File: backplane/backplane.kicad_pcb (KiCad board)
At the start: 2 copper layers, 100 x 100 mm, 14 parts, among them J1 Conn_02x16_Row_Letter_First, J2 Conn_02x16_Row_Letter_First, J3 Conn_02x16_Row_Letter_First, J4 Conn_02x16_Row_Letter_First, J5 Conn_02x16_Row_Letter_First

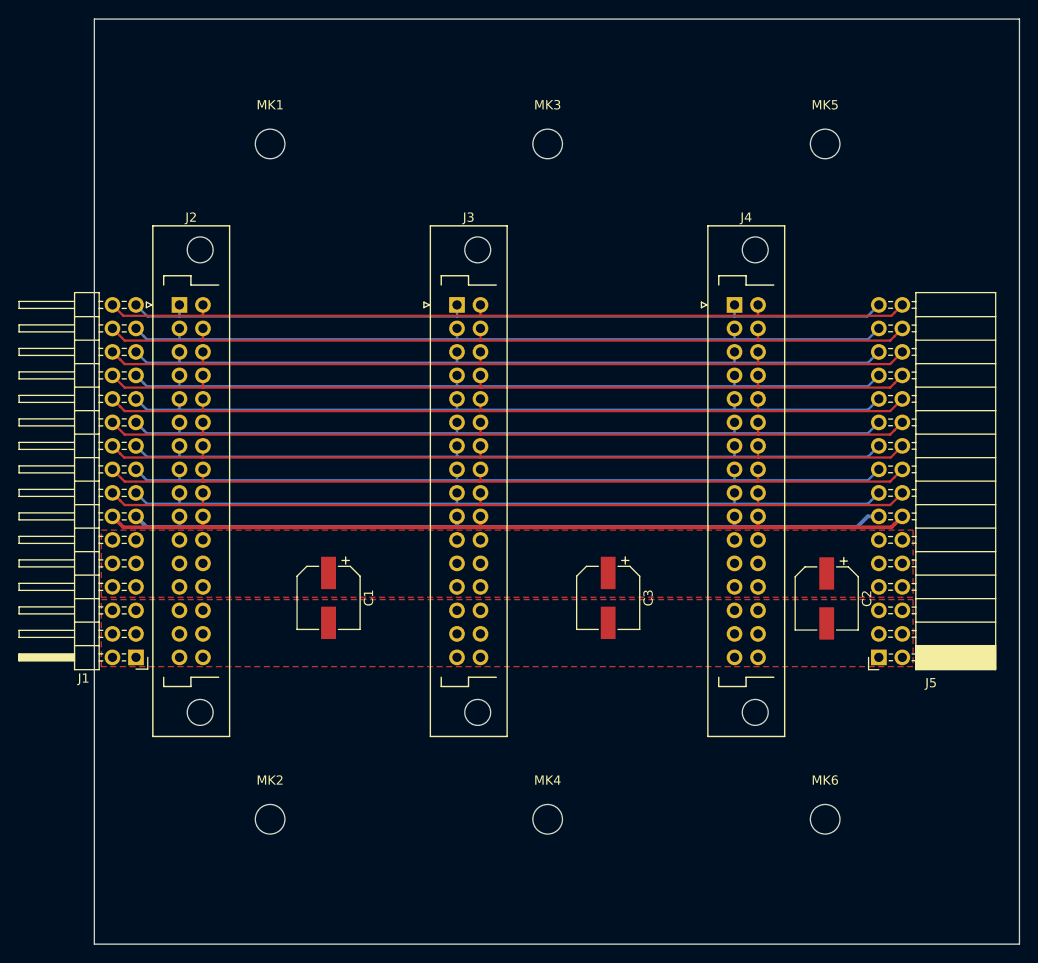
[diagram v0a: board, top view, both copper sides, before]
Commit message: move right side by 10mm so you can actually chain stuff
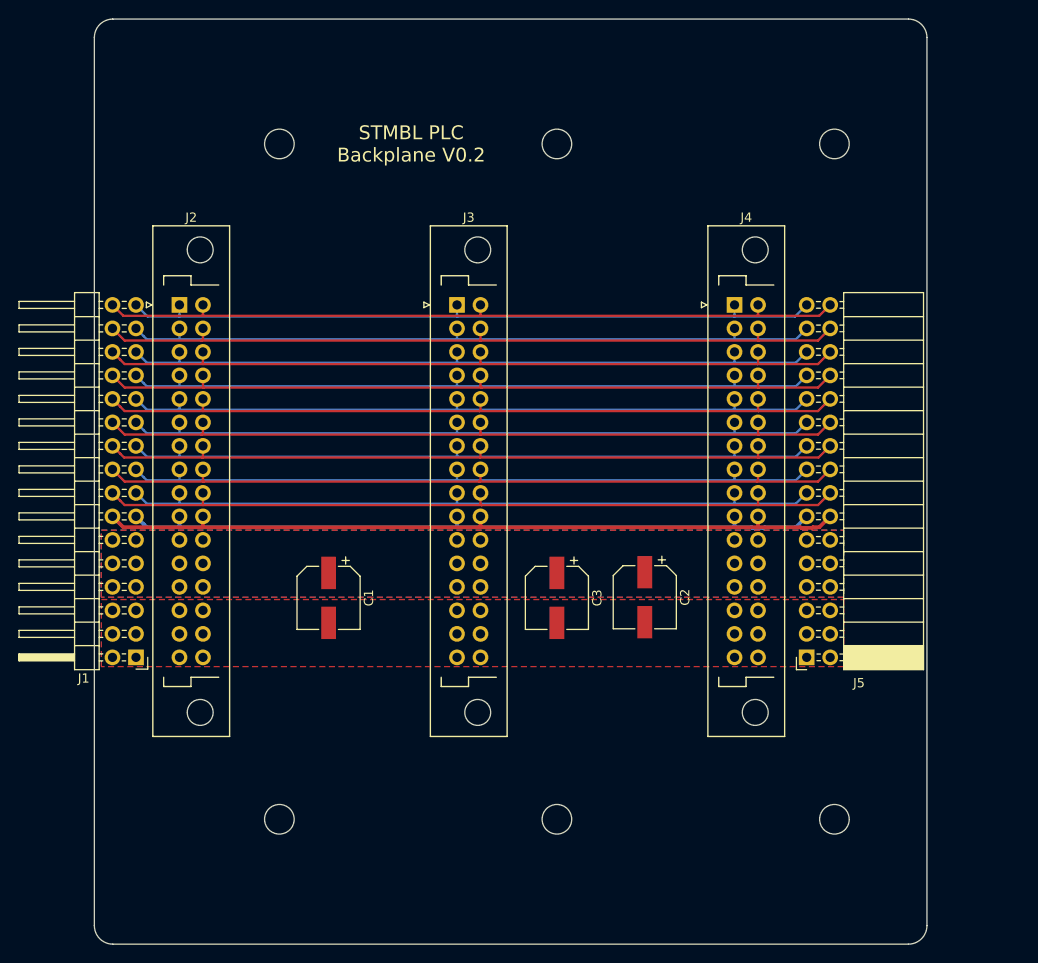
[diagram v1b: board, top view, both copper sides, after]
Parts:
- moved C2 19.7 mm to (149.5, 107.5)
- moved J5 7.80 mm to (167.0, 114.0)
- moved C3 5.54 mm to (140.0, 107.6)
- moved MK1 1.00 mm to (110.0, 58.5)
- moved MK2 1.00 mm to (110.0, 131.5)
- moved MK3 1.00 mm to (140.0, 58.5)
- moved MK4 1.00 mm to (140.0, 131.5)
- moved MK5 1.00 mm to (170.0, 58.5)
- moved MK6 1.00 mm to (170.0, 131.5)
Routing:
- net PIN8: track 84.9 -> 77.1 mm
- net PIN6: track 84.8 -> 77.0 mm
- net PIN5: track 84.9 -> 77.1 mm
- net PIN4: track 84.9 -> 77.1 mm
- net PIN3: track 84.8 -> 77.0 mm
- net PIN2: track 84.8 -> 77.0 mm
- net PIN16: track 90.5 -> 82.7 mm
- net PIN15: track 90.5 -> 82.7 mm
- net PIN13: track 90.5 -> 82.7 mm
- net PIN12: track 90.5 -> 82.7 mm
- net PIN9: track 84.9 -> 77.1 mm
- net PIN7: track 84.9 -> 77.1 mm
- net PIN19: track 90.5 -> 82.7 mm
- net PIN18: track 90.5 -> 82.7 mm
- net PIN11: track 90.0 -> 82.2 mm
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- added copper zone on B.Cu, net +24V
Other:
- board size 100 x 100 mm -> 90 x 100 mm
- board text added: "STMBL PLC Backplane V0.2"

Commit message: change over to plc bus
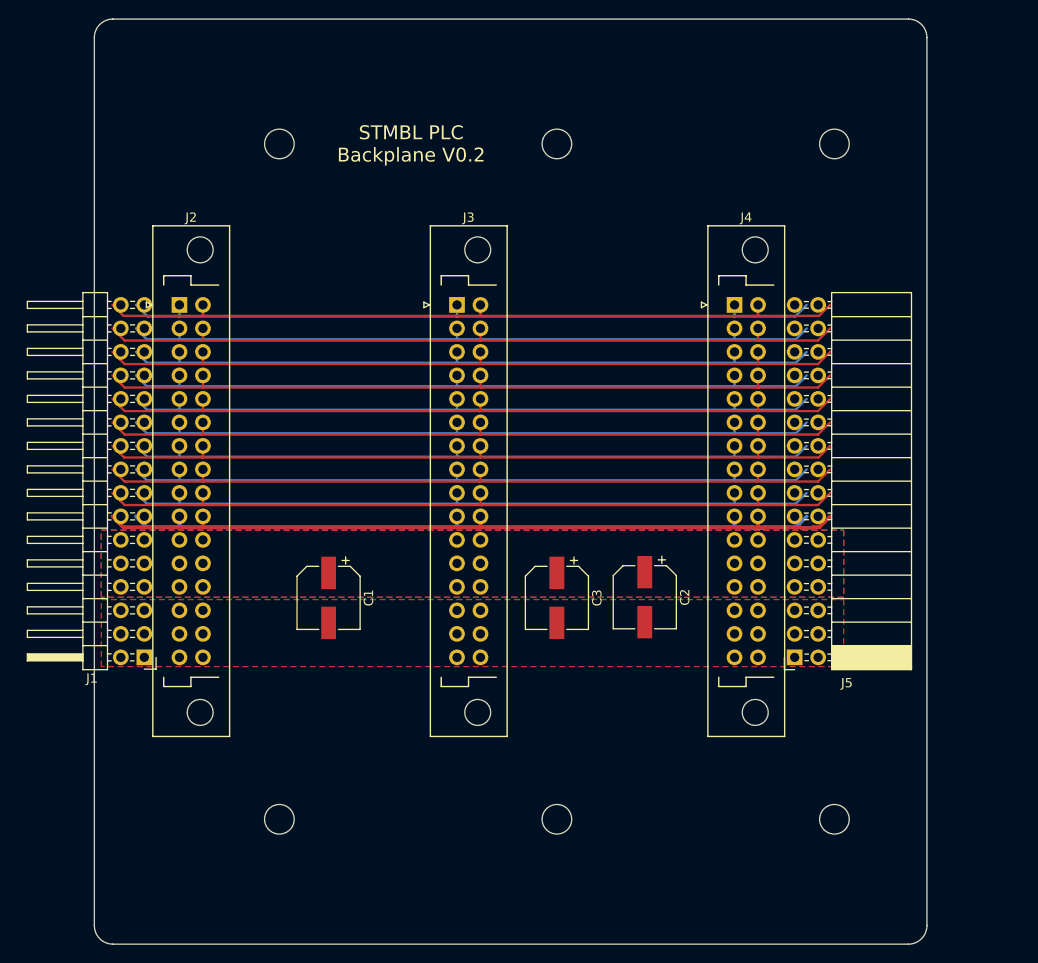
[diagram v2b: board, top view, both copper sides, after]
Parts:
- moved J5 1.30 mm to (165.7, 114.0)
- moved J1 0.90 mm to (95.4, 114.0)
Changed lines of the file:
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@@
   )
   (module Connector_PinHeader_2.54mm:PinHeader_2x16_P2.54mm_Horizontal (layer F.Cu)
-    (at 94.5 114 180)
+    (at 95.4 114 180)
     (descr "Through hole angled pin header, 2x16, 2.54mm pitch, 6mm pin length, double rows")
     (tags "Through hole angled pin header THT 2x16 2.54mm double row")
@@
   )
   (module Connector_PinSocket_2.54mm:PinSocket_2x16_P2.54mm_Horizontal (layer F.Cu)
-    (at 167 114 180)
+    (at 165.7 114 180)
     (descr "Through hole angled socket strip, 2x16, 2.54mm pitch, 8.51mm socket length, double cols (from Kicad 4.0.7), script generated")
     (tags "Through hole angled socket strip THT 2x16 2.54mm double row")
@@
     (connect_pads (clearance 0.2))
     (min_thickness 0.2)
-    (fill yes (arc_segments 32) (thermal_gap 0.254) (thermal_bridge_width 0.5))
+    (fill (arc_segments 32) (thermal_gap 0.254) (thermal_bridge_width 0.5))
     (polygon
       (pts
@@
     (connect_pads (clearance 0.2))
     (min_thickness 0.2)
-    (fill yes (arc_segments 32) (thermal_gap 0.254) (thermal_bridge_width 0.5))
+    (fill (arc_segments 32) (thermal_gap 0.254) (thermal_bridge_width 0.5))
     (polygon
       (pts
@@
     (connect_pads (clearance 0.2))
     (min_thickness 0.2)
-    (fill yes (arc_segments 32) (thermal_gap 0.254) (thermal_bridge_width 0.5))
+    (fill (arc_segments 32) (thermal_gap 0.254) (thermal_bridge_width 0.5))
     (polygon
       (pts

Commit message: adjust backplane to new spec
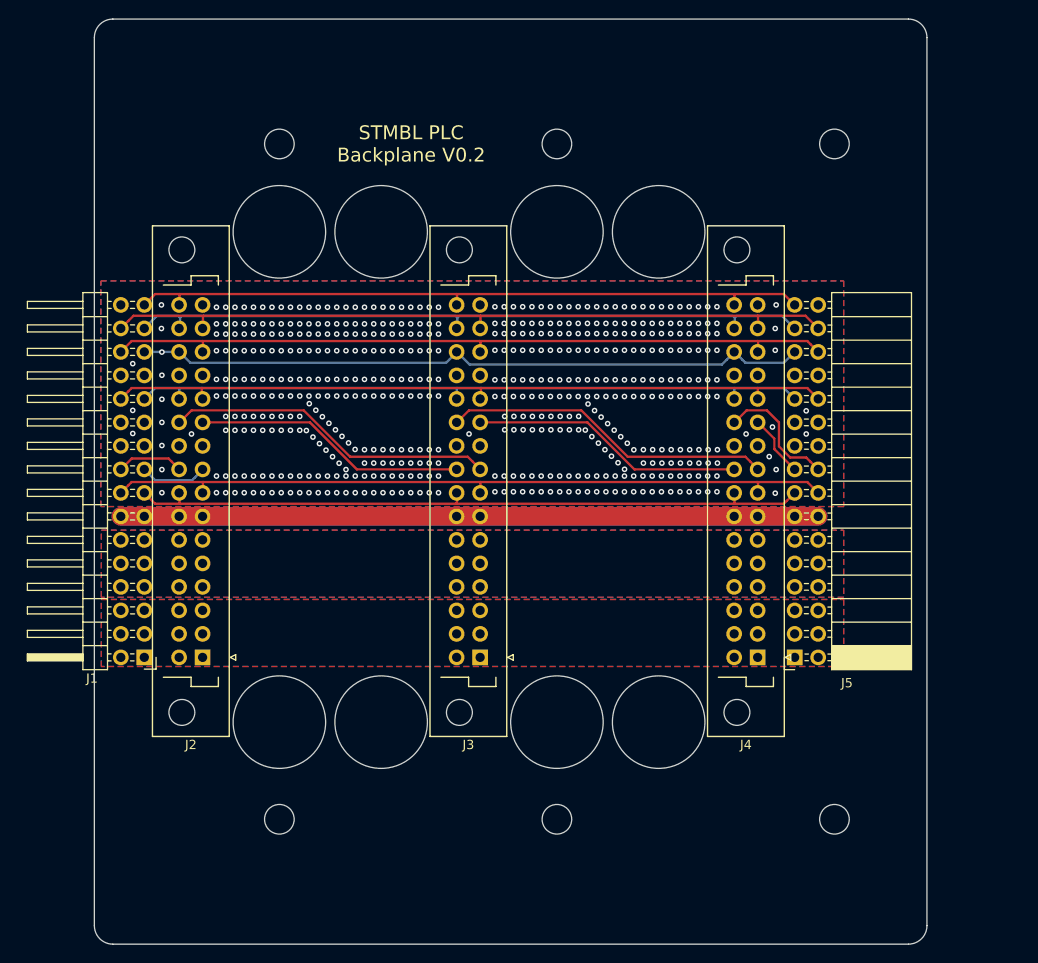
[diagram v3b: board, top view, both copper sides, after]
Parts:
- removed C1, C2, C3: CP, Capacitor_SMD:CP_Elec_6.3x7.7
- moved J2 38.2 mm to (101.7, 114.0), turned to 180 degrees
- moved J3 38.2 mm to (131.7, 114.0), turned to 180 degrees
- moved J4 38.2 mm to (161.7, 114.0), turned to 180 degrees
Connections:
- J1 pad 1: GNDPWR -> VDC
- J1 pad 10: +24V -> GNDPWR
- J1 pad 11: +24V -> GNDPWR
- J1 pad 12: +24V -> GNDPWR
- J1 pad 13: PIN10 -> +24V
- J1 pad 14: PIN20 -> +24V
- J1 pad 15: PIN9 -> LSC+
- J1 pad 16: PIN19 -> LSC-
- J1 pad 17: PIN8 -> Net-(J1-Pad17)
- J1 pad 18: PIN18 -> Net-(J1-Pad18)
- J1 pad 19: PIN7 -> GND
- J1 pad 2: GNDPWR -> VDC
- J1 pad 20: PIN17 -> GND
- J1 pad 21: PIN6 -> Net-(J1-Pad21)
- J1 pad 22: PIN16 -> Net-(J1-Pad22)
- J1 pad 23: PIN5 -> LMI-
- J1 pad 24: PIN15 -> LMI+
- J1 pad 25: PIN4 -> GND
- J1 pad 26: PIN14 -> GND
- J1 pad 27: PIN3 -> LCS+
- J1 pad 28: PIN13 -> LCS-
- J1 pad 29: PIN2 -> UA1+
- J1 pad 3: GNDPWR -> VDC
- J1 pad 30: PIN12 -> UA1-
- J1 pad 31: PIN1 -> EST
- J1 pad 32: PIN11 -> GND
- J1 pad 4: GNDPWR -> VDC
- J1 pad 5: GNDPWR -> VDC
- J1 pad 6: GNDPWR -> VDC
- J1 pad 7: +24V -> GNDPWR
- J1 pad 8: +24V -> GNDPWR
- J1 pad 9: +24V -> GNDPWR
- J2 pad a1: PIN1 -> VDC
- J2 pad a10: PIN10 -> GND
- J2 pad a11: +24V -> Net-(J2-Pada11)
- J2 pad a12: +24V -> LMI+
- J2 pad a13: +24V -> GND
- J2 pad a14: GNDPWR -> LCS-
- J2 pad a15: GNDPWR -> UA1-
- J2 pad a16: GNDPWR -> GND
- J2 pad a2: PIN2 -> VDC
- J2 pad a3: PIN3 -> VDC
- J2 pad a4: PIN4 -> GNDPWR
- J2 pad a5: PIN5 -> GNDPWR
- J2 pad a6: PIN6 -> GNDPWR
- J2 pad a7: PIN7 -> +24V
- J2 pad a8: PIN8 -> LSC-
- J2 pad a9: PIN9 -> Net-(J1-Pad17)
- J2 pad b1: PIN11 -> VDC
- J2 pad b10: PIN20 -> GND
- J2 pad b11: +24V -> Net-(J2-Padb11)
- J2 pad b12: +24V -> LMI-
- J2 pad b13: +24V -> GND
- J2 pad b14: GNDPWR -> LCS+
- J2 pad b15: GNDPWR -> UA1+
- J2 pad b16: GNDPWR -> EST
- J2 pad b2: PIN12 -> VDC
- J2 pad b3: PIN13 -> VDC
- J2 pad b4: PIN14 -> GNDPWR
- J2 pad b5: PIN15 -> GNDPWR
- J2 pad b6: PIN16 -> GNDPWR
- J2 pad b7: PIN17 -> +24V
- J2 pad b8: PIN18 -> LSC+
- J2 pad b9: PIN19 -> Net-(J1-Pad18)
- J3 pad a1: PIN1 -> VDC
- J3 pad a10: PIN10 -> GND
- J3 pad a11: +24V -> Net-(J3-Pada11)
- J3 pad a12: +24V -> LMI+
- J3 pad a13: +24V -> GND
- J3 pad a14: GNDPWR -> LCS-
- J3 pad a15: GNDPWR -> UA1-
- J3 pad a16: GNDPWR -> GND
- J3 pad a2: PIN2 -> VDC
- J3 pad a3: PIN3 -> VDC
- J3 pad a4: PIN4 -> GNDPWR
- J3 pad a5: PIN5 -> GNDPWR
- J3 pad a6: PIN6 -> GNDPWR
- J3 pad a7: PIN7 -> +24V
- J3 pad a8: PIN8 -> LSC-
- J3 pad a9: PIN9 -> Net-(J2-Padb11)
- J3 pad b1: PIN11 -> VDC
- J3 pad b10: PIN20 -> GND
- J3 pad b11: +24V -> Net-(J3-Padb11)
- J3 pad b12: +24V -> LMI-
- J3 pad b13: +24V -> GND
- J3 pad b14: GNDPWR -> LCS+
- J3 pad b15: GNDPWR -> UA1+
- J3 pad b16: GNDPWR -> EST
- J3 pad b2: PIN12 -> VDC
- J3 pad b3: PIN13 -> VDC
- J3 pad b4: PIN14 -> GNDPWR
- J3 pad b5: PIN15 -> GNDPWR
- J3 pad b6: PIN16 -> GNDPWR
- J3 pad b7: PIN17 -> +24V
- J3 pad b8: PIN18 -> LSC+
- J3 pad b9: PIN19 -> Net-(J2-Pada11)
- J4 pad a1: PIN1 -> VDC
- J4 pad a10: PIN10 -> GND
- J4 pad a11: +24V -> Net-(J4-Pada11)
- J4 pad a12: +24V -> LMI+
- J4 pad a13: +24V -> GND
- J4 pad a14: GNDPWR -> LCS-
- J4 pad a15: GNDPWR -> UA1-
- J4 pad a16: GNDPWR -> GND
- J4 pad a2: PIN2 -> VDC
- J4 pad a3: PIN3 -> VDC
- J4 pad a4: PIN4 -> GNDPWR
- J4 pad a5: PIN5 -> GNDPWR
- J4 pad a6: PIN6 -> GNDPWR
- J4 pad a7: PIN7 -> +24V
- J4 pad a8: PIN8 -> LSC-
- J4 pad a9: PIN9 -> Net-(J3-Padb11)
- J4 pad b1: PIN11 -> VDC
- J4 pad b10: PIN20 -> GND
- J4 pad b11: +24V -> Net-(J4-Padb11)
- J4 pad b12: +24V -> LMI-
- J4 pad b13: +24V -> GND
- J4 pad b14: GNDPWR -> LCS+
- J4 pad b15: GNDPWR -> UA1+
- J4 pad b16: GNDPWR -> EST
- J4 pad b2: PIN12 -> VDC
- J4 pad b3: PIN13 -> VDC
- J4 pad b4: PIN14 -> GNDPWR
- J4 pad b5: PIN15 -> GNDPWR
- J4 pad b6: PIN16 -> GNDPWR
- J4 pad b7: PIN17 -> +24V
- J4 pad b8: PIN18 -> LSC+
- J4 pad b9: PIN19 -> Net-(J3-Pada11)
- J5 pad 1: GNDPWR -> VDC
- J5 pad 10: +24V -> GNDPWR
- J5 pad 11: +24V -> GNDPWR
- J5 pad 12: +24V -> GNDPWR
- J5 pad 13: PIN10 -> +24V
- J5 pad 14: PIN20 -> +24V
- J5 pad 15: PIN9 -> LSC+
- J5 pad 16: PIN19 -> LSC-
- J5 pad 17: PIN8 -> Net-(J4-Pada11)
- J5 pad 18: PIN18 -> Net-(J4-Padb11)
- J5 pad 19: PIN7 -> GND
- J5 pad 2: GNDPWR -> VDC
- J5 pad 20: PIN17 -> GND
- J5 pad 21: PIN6 -> Net-(J5-Pad21)
- J5 pad 22: PIN16 -> Net-(J5-Pad22)
- J5 pad 23: PIN5 -> LMI-
- J5 pad 24: PIN15 -> LMI+
- J5 pad 25: PIN4 -> GND
- J5 pad 26: PIN14 -> GND
- J5 pad 27: PIN3 -> LCS+
- J5 pad 28: PIN13 -> LCS-
- J5 pad 29: PIN2 -> UA1+
- J5 pad 3: GNDPWR -> VDC
- J5 pad 30: PIN12 -> UA1-
- J5 pad 31: PIN1 -> EST
- J5 pad 32: PIN11 -> GND
- J5 pad 4: GNDPWR -> VDC
- J5 pad 5: GNDPWR -> VDC
- J5 pad 6: GNDPWR -> VDC
- J5 pad 7: +24V -> GNDPWR
- J5 pad 8: +24V -> GNDPWR
- J5 pad 9: +24V -> GNDPWR
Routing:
- net +24V: track 0.00 -> 150.8 mm
- net PIN18: track 82.7 -> 0.00 mm
- net PIN16: track 82.7 -> 0.00 mm
- net PIN12: track 82.7 -> 0.00 mm
- net PIN19: track 82.7 -> 0.00 mm
- net PIN14: track 82.7 -> 0.00 mm
- net PIN15: track 82.7 -> 0.00 mm
- net PIN13: track 82.7 -> 0.00 mm
- net PIN17: track 82.5 -> 0.00 mm
- net PIN20: track 82.2 -> 0.00 mm
- net PIN11: track 82.2 -> 0.00 mm
- net UA1-: track 0.00 -> 80.6 mm
- net LCS-: track 0.00 -> 80.0 mm
- net LMI+: track 0.00 -> 80.0 mm
- net LSC-: track 0.00 -> 79.9 mm
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- added copper zone on B.Cu, net GND
- added copper zone on F.Cu, net GND
- added copper zone on B.Cu, net GNDPWR
- added copper zone on B.Cu, net VDC
- added copper zone on F.Cu, net VDC
- removed copper zone on B.Cu, net +24V
- removed copper zone on F.Cu, net +24V
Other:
- outline, holes or cut-outs redrawn
